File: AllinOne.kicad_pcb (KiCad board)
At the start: 2 copper layers, 24 parts, among them SW0 SW_Push, SW1 SW_Push, SW2 SW_Push, SW3 SW_Push, U1 ATmega32U4-A, Y1 16MHz

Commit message: Started organizing switches
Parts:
- removed D2, D3, D4: SOD-123, Diode_SMD:D_SOD-123
- added D10: SOD-123, Diode_SMD:D_SOD-123, F.Cu at (370.4, 227.7)
- added D100: SOD-123, Diode_SMD:D_SOD-123, F.Cu at (405.2, 227.7)
- added D101: SOD-123, Diode_SMD:D_SOD-123, F.Cu at (405.2, 231.0)
- added D102: SOD-123, Diode_SMD:D_SOD-123, F.Cu at (405.2, 234.4)
- added D103: SOD-123, Diode_SMD:D_SOD-123, F.Cu at (405.2, 237.7)
- added D104: SOD-123, Diode_SMD:D_SOD-123, F.Cu at (405.2, 241.1)
- added D105: SOD-123, Diode_SMD:D_SOD-123, F.Cu at (405.2, 244.4)
- added D106: SOD-123, Diode_SMD:D_SOD-123, F.Cu at (405.2, 247.8)
- added D107: SOD-123, Diode_SMD:D_SOD-123, F.Cu at (405.2, 251.1)
- added D108: SOD-123, Diode_SMD:D_SOD-123, F.Cu at (411.0, 207.6)
- added D109: SOD-123, Diode_SMD:D_SOD-123, F.Cu at (411.0, 210.9)
- added D11: SOD-123, Diode_SMD:D_SOD-123, F.Cu at (370.4, 231.0)
- added D110: SOD-123, Diode_SMD:D_SOD-123, F.Cu at (411.0, 214.3)
- added D111: SOD-123, Diode_SMD:D_SOD-123, F.Cu at (411.0, 217.6)
- added D112: SOD-123, Diode_SMD:D_SOD-123, F.Cu at (411.0, 221.0)
- added D113: SOD-123, Diode_SMD:D_SOD-123, F.Cu at (411.0, 224.3)
- added D114: SOD-123, Diode_SMD:D_SOD-123, F.Cu at (411.0, 227.7)
- added D115: SOD-123, Diode_SMD:D_SOD-123, F.Cu at (411.0, 231.0)
- added D116: SOD-123, Diode_SMD:D_SOD-123, F.Cu at (411.0, 234.4)
- added D119: SOD-123, Diode_SMD:D_SOD-123, F.Cu at (411.0, 237.7)
- added D12: SOD-123, Diode_SMD:D_SOD-123, F.Cu at (370.4, 234.4)
- added D121: SOD-123, Diode_SMD:D_SOD-123, F.Cu at (411.0, 241.1)
- added D122: SOD-123, Diode_SMD:D_SOD-123, F.Cu at (411.0, 244.4)
- added D123: SOD-123, Diode_SMD:D_SOD-123, F.Cu at (411.0, 247.8)
- added D124: SOD-123, Diode_SMD:D_SOD-123, F.Cu at (411.0, 251.1)
- added D125: SOD-123, Diode_SMD:D_SOD-123, F.Cu at (416.8, 207.6)
- added D126: SOD-123, Diode_SMD:D_SOD-123, F.Cu at (416.8, 210.9)
- added D127: SOD-123, Diode_SMD:D_SOD-123, F.Cu at (416.8, 214.3)
- added D13: SOD-123, Diode_SMD:D_SOD-123, F.Cu at (370.4, 237.7)
- added D131: SOD-123, Diode_SMD:D_SOD-123, F.Cu at (416.8, 217.6)
- added D135: SOD-123, Diode_SMD:D_SOD-123, F.Cu at (416.8, 221.0)
- added D136: SOD-123, Diode_SMD:D_SOD-123, F.Cu at (416.8, 224.3)
- added D137: SOD-123, Diode_SMD:D_SOD-123, F.Cu at (416.8, 227.7)
- added D138: SOD-123, Diode_SMD:D_SOD-123, F.Cu at (416.8, 231.0)
- added D139: SOD-123, Diode_SMD:D_SOD-123, F.Cu at (416.8, 234.4)
- added D14: SOD-123, Diode_SMD:D_SOD-123, F.Cu at (370.4, 241.1)
- added D140: SOD-123, Diode_SMD:D_SOD-123, F.Cu at (416.8, 237.7)
- added D141: SOD-123, Diode_SMD:D_SOD-123, F.Cu at (416.8, 241.1)
- added D142: SOD-123, Diode_SMD:D_SOD-123, F.Cu at (416.8, 244.4)
- added D143: SOD-123, Diode_SMD:D_SOD-123, F.Cu at (416.8, 247.8)
- added D144: SOD-123, Diode_SMD:D_SOD-123, F.Cu at (416.8, 251.1)
- added D15: SOD-123, Diode_SMD:D_SOD-123, F.Cu at (370.4, 244.4)
- added D16: SOD-123, Diode_SMD:D_SOD-123, F.Cu at (370.4, 247.8)
- added D17: SOD-123, Diode_SMD:D_SOD-123, F.Cu at (370.4, 251.1)
- added D18: SOD-123, Diode_SMD:D_SOD-123, F.Cu at (376.2, 207.6)
- added D19: SOD-123, Diode_SMD:D_SOD-123, F.Cu at (376.2, 210.9)
- added D20: SOD-123, Diode_SMD:D_SOD-123, F.Cu at (376.2, 214.3)
- added D23: SOD-123, Diode_SMD:D_SOD-123, F.Cu at (376.2, 217.6)
- added D24: SOD-123, Diode_SMD:D_SOD-123, F.Cu at (376.2, 221.0)
- added D25: SOD-123, Diode_SMD:D_SOD-123, F.Cu at (376.2, 224.3)
- added D26: SOD-123, Diode_SMD:D_SOD-123, F.Cu at (376.2, 227.7)
- added D27: SOD-123, Diode_SMD:D_SOD-123, F.Cu at (376.2, 231.0)
- added D28: SOD-123, Diode_SMD:D_SOD-123, F.Cu at (376.2, 234.4)
- added D29: SOD-123, Diode_SMD:D_SOD-123, F.Cu at (376.2, 237.7)
- added D30: SOD-123, Diode_SMD:D_SOD-123, F.Cu at (376.2, 241.1)
- added D31: SOD-123, Diode_SMD:D_SOD-123, F.Cu at (376.2, 244.4)
- added D32: SOD-123, Diode_SMD:D_SOD-123, F.Cu at (376.2, 247.8)
- added D33: SOD-123, Diode_SMD:D_SOD-123, F.Cu at (376.2, 251.1)
- added D34: SOD-123, Diode_SMD:D_SOD-123, F.Cu at (382.0, 207.6)
- added D35: SOD-123, Diode_SMD:D_SOD-123, F.Cu at (382.0, 210.9)
- added D36: SOD-123, Diode_SMD:D_SOD-123, F.Cu at (382.0, 214.3)
- added D37: SOD-123, Diode_SMD:D_SOD-123, F.Cu at (382.0, 217.6)
- added D38: SOD-123, Diode_SMD:D_SOD-123, F.Cu at (382.0, 221.0)
- added D39: SOD-123, Diode_SMD:D_SOD-123, F.Cu at (382.0, 224.3)
- added D40: SOD-123, Diode_SMD:D_SOD-123, F.Cu at (382.0, 227.7)
- added D41: SOD-123, Diode_SMD:D_SOD-123, F.Cu at (382.0, 231.0)
- added D42: SOD-123, Diode_SMD:D_SOD-123, F.Cu at (382.0, 234.4)
- added D43: SOD-123, Diode_SMD:D_SOD-123, F.Cu at (382.0, 237.7)
- added D44: SOD-123, Diode_SMD:D_SOD-123, F.Cu at (382.0, 241.1)
- added D45: SOD-123, Diode_SMD:D_SOD-123, F.Cu at (382.0, 244.4)
- added D46: SOD-123, Diode_SMD:D_SOD-123, F.Cu at (382.0, 247.8)
- added D47: SOD-123, Diode_SMD:D_SOD-123, F.Cu at (382.0, 251.1)
- added D48: SOD-123, Diode_SMD:D_SOD-123, F.Cu at (387.8, 207.6)
- added D49: SOD-123, Diode_SMD:D_SOD-123, F.Cu at (387.8, 210.9)
- added D5: SOD-123, Diode_SMD:D_SOD-123, F.Cu at (370.4, 210.9)
- added D50: SOD-123, Diode_SMD:D_SOD-123, F.Cu at (387.8, 214.3)
- added D51: SOD-123, Diode_SMD:D_SOD-123, F.Cu at (387.8, 217.6)
- added D52: SOD-123, Diode_SMD:D_SOD-123, F.Cu at (387.8, 221.0)
- added D53: SOD-123, Diode_SMD:D_SOD-123, F.Cu at (387.8, 224.3)
- added D54: SOD-123, Diode_SMD:D_SOD-123, F.Cu at (387.8, 227.7)
- added D55: SOD-123, Diode_SMD:D_SOD-123, F.Cu at (387.8, 231.0)
- added D56: SOD-123, Diode_SMD:D_SOD-123, F.Cu at (387.8, 234.4)
- added D57: SOD-123, Diode_SMD:D_SOD-123, F.Cu at (387.8, 237.7)
- added D58: SOD-123, Diode_SMD:D_SOD-123, F.Cu at (387.8, 241.1)
- added D6: SOD-123, Diode_SMD:D_SOD-123, F.Cu at (370.4, 214.3)
- added D60: SOD-123, Diode_SMD:D_SOD-123, F.Cu at (387.8, 244.4)
- added D61: SOD-123, Diode_SMD:D_SOD-123, F.Cu at (387.8, 247.8)
- added D62: SOD-123, Diode_SMD:D_SOD-123, F.Cu at (387.8, 251.1)
- added D63: SOD-123, Diode_SMD:D_SOD-123, F.Cu at (393.6, 207.6)
- added D64: SOD-123, Diode_SMD:D_SOD-123, F.Cu at (393.6, 210.9)
- added D65: SOD-123, Diode_SMD:D_SOD-123, F.Cu at (393.6, 214.3)
- added D66: SOD-123, Diode_SMD:D_SOD-123, F.Cu at (393.6, 217.6)
- added D67: SOD-123, Diode_SMD:D_SOD-123, F.Cu at (393.6, 221.0)
- added D68: SOD-123, Diode_SMD:D_SOD-123, F.Cu at (393.6, 224.3)
- added D69: SOD-123, Diode_SMD:D_SOD-123, F.Cu at (393.6, 227.7)
- added D7: SOD-123, Diode_SMD:D_SOD-123, F.Cu at (370.4, 217.6)
- added D70: SOD-123, Diode_SMD:D_SOD-123, F.Cu at (393.6, 231.0)
- added D71: SOD-123, Diode_SMD:D_SOD-123, F.Cu at (393.6, 234.4)
- added D72: SOD-123, Diode_SMD:D_SOD-123, F.Cu at (393.6, 237.7)
- added D73: SOD-123, Diode_SMD:D_SOD-123, F.Cu at (393.6, 241.1)
- added D74: SOD-123, Diode_SMD:D_SOD-123, F.Cu at (393.6, 244.4)
- added D75: SOD-123, Diode_SMD:D_SOD-123, F.Cu at (393.6, 247.8)
- added D76: SOD-123, Diode_SMD:D_SOD-123, F.Cu at (393.6, 251.1)
- added D77: SOD-123, Diode_SMD:D_SOD-123, F.Cu at (399.4, 207.6)
- added D79: SOD-123, Diode_SMD:D_SOD-123, F.Cu at (399.4, 210.9)
- added D8: SOD-123, Diode_SMD:D_SOD-123, F.Cu at (370.4, 221.0)
- added D80: SOD-123, Diode_SMD:D_SOD-123, F.Cu at (399.4, 214.3)
- added D81: SOD-123, Diode_SMD:D_SOD-123, F.Cu at (399.4, 217.6)
- added D82: SOD-123, Diode_SMD:D_SOD-123, F.Cu at (399.4, 221.0)
- added D83: SOD-123, Diode_SMD:D_SOD-123, F.Cu at (399.4, 224.3)
- added D84: SOD-123, Diode_SMD:D_SOD-123, F.Cu at (399.4, 227.7)
- added D85: SOD-123, Diode_SMD:D_SOD-123, F.Cu at (399.4, 231.0)
- added D86: SOD-123, Diode_SMD:D_SOD-123, F.Cu at (399.4, 234.4)
- added D87: SOD-123, Diode_SMD:D_SOD-123, F.Cu at (399.4, 237.7)
- added D88: SOD-123, Diode_SMD:D_SOD-123, F.Cu at (399.4, 241.1)
- added D89: SOD-123, Diode_SMD:D_SOD-123, F.Cu at (399.4, 244.4)
- added D9: SOD-123, Diode_SMD:D_SOD-123, F.Cu at (370.4, 224.3)
- added D90: SOD-123, Diode_SMD:D_SOD-123, F.Cu at (399.4, 247.8)
- added D91: SOD-123, Diode_SMD:D_SOD-123, F.Cu at (399.4, 251.1)
- added D92: SOD-123, Diode_SMD:D_SOD-123, F.Cu at (405.2, 207.6)
- added D93: SOD-123, Diode_SMD:D_SOD-123, F.Cu at (405.2, 210.9)
- added D94: SOD-123, Diode_SMD:D_SOD-123, F.Cu at (405.2, 214.3)
- added D95: SOD-123, Diode_SMD:D_SOD-123, F.Cu at (405.2, 217.6)
- added D96: SOD-123, Diode_SMD:D_SOD-123, F.Cu at (405.2, 221.0)
- added D97: SOD-123, Diode_SMD:D_SOD-123, F.Cu at (405.2, 224.3)
- added SW10: SW_Push, Button_Switch_Keyboard:SW_Cherry_MX_1.00u_PCB, F.Cu at (226.1, 87.2)
- added SW100: SW_Push, Button_Switch_Keyboard:SW_Cherry_MX_1.00u_PCB, F.Cu at (319.5, 168.6)
- added SW101: SW_Push, Button_Switch_Keyboard:SW_Cherry_MX_1.00u_PCB, F.Cu at (319.5, 188.8)
- added SW102: SW_Push, Button_Switch_Keyboard:SW_Cherry_MX_1.00u_PCB, F.Cu at (319.5, 209.0)
- added SW103: SW_Push, Button_Switch_Keyboard:SW_Cherry_MX_1.00u_PCB, F.Cu at (319.5, 229.2)
- added SW104: SW_Push, Button_Switch_Keyboard:SW_Cherry_MX_1.00u_PCB, F.Cu at (319.5, 249.4)
- added SW105: SW_Push, Button_Switch_Keyboard:SW_Cherry_MX_1.00u_PCB, F.Cu at (319.5, 269.6)
- added SW106: SW_Push, Button_Switch_Keyboard:SW_Cherry_MX_1.00u_PCB, F.Cu at (319.5, 289.8)
- added SW107: SW_Push, Button_Switch_Keyboard:SW_Cherry_MX_1.00u_PCB, F.Cu at (319.5, 310.0)
- added SW108: SW_Push, Button_Switch_Keyboard:SW_Cherry_MX_1.00u_PCB, F.Cu at (319.5, 330.2)
- added SW109: SW_Push, Button_Switch_Keyboard:SW_Cherry_MX_1.00u_PCB, F.Cu at (319.5, 350.4)
- added SW11: SW_Push, Button_Switch_Keyboard:SW_Cherry_MX_1.00u_PCB, F.Cu at (245.1, 87.2)
- added SW110: SW_Push, Button_Switch_Keyboard:SW_Cherry_MX_1.00u_PCB, F.Cu at (319.5, 370.6)
- added SW111: SW_Push, Button_Switch_Keyboard:SW_Cherry_MX_1.00u_PCB, F.Cu at (319.5, 390.8)
- added SW114: SW_Push, Button_Switch_Keyboard:SW_Cherry_MX_1.00u_PCB, F.Cu at (339.5, 144.4)
- added SW116: SW_Push, Button_Switch_Keyboard:SW_Cherry_MX_1.00u_PCB, F.Cu at (339.7, 168.6)
- added SW117: SW_Push, Button_Switch_Keyboard:SW_Cherry_MX_1.00u_PCB, F.Cu at (339.7, 188.8)
- added SW118: SW_Push, Button_Switch_Keyboard:SW_Cherry_MX_1.00u_PCB, F.Cu at (339.7, 209.0)
- added SW119: SW_Push, Button_Switch_Keyboard:SW_Cherry_MX_1.00u_PCB, F.Cu at (339.7, 229.2)
- added SW12: SW_Push, Button_Switch_Keyboard:SW_Cherry_MX_1.00u_PCB, F.Cu at (264.2, 87.2)
- added SW120: SW_Push, Button_Switch_Keyboard:SW_Cherry_MX_1.00u_PCB, F.Cu at (339.7, 249.4)
- added SW121: SW_Push, Button_Switch_Keyboard:SW_Cherry_MX_1.00u_PCB, F.Cu at (339.7, 269.6)
- added SW122: SW_Push, Button_Switch_Keyboard:SW_Cherry_MX_1.00u_PCB, F.Cu at (339.7, 289.8)
- added SW126: SW_Push, Button_Switch_Keyboard:SW_Cherry_MX_6.25u_PCB, F.Cu at (228.1, 411.0)
- added SW13: SW_Push, Button_Switch_Keyboard:SW_Cherry_MX_1.00u_PCB, F.Cu at (283.2, 87.2)
- added SW130: SW_Push, Button_Switch_Keyboard:SW_Cherry_MX_1.00u_PCB, F.Cu at (339.7, 310.0)
- added SW131: SW_Push, Button_Switch_Keyboard:SW_Cherry_MX_1.00u_PCB, F.Cu at (339.7, 330.2)
- added SW132: SW_Push, Button_Switch_Keyboard:SW_Cherry_MX_1.00u_PCB, F.Cu at (339.7, 350.4)
- added SW133: SW_Push, Button_Switch_Keyboard:SW_Cherry_MX_1.00u_PCB, F.Cu at (339.7, 370.6)
- added SW134: SW_Push, Button_Switch_Keyboard:SW_Cherry_MX_1.00u_PCB, F.Cu at (339.7, 390.8)
- added SW135: SW_Push, Button_Switch_Keyboard:SW_Cherry_MX_1.00u_PCB, F.Cu at (358.5, 144.4)
- added SW136: SW_Push, Button_Switch_Keyboard:SW_Cherry_MX_1.00u_PCB, F.Cu at (359.9, 168.6)
- added SW137: SW_Push, Button_Switch_Keyboard:SW_Cherry_MX_1.00u_PCB, F.Cu at (359.9, 188.8)
- added SW138: SW_Push, Button_Switch_Keyboard:SW_Cherry_MX_1.00u_PCB, F.Cu at (359.9, 209.0)
- added SW139: SW_Push, Button_Switch_Keyboard:SW_Cherry_MX_1.00u_PCB, F.Cu at (359.9, 229.2)
- added SW14: SW_Push, Button_Switch_Keyboard:SW_Cherry_MX_1.00u_PCB, F.Cu at (302.3, 87.2)
- added SW15: SW_Push, Button_Switch_Keyboard:SW_Cherry_MX_1.00u_PCB, F.Cu at (321.3, 87.2)
- added SW16: SW_Push, Button_Switch_Keyboard:SW_Cherry_MX_2.00u_PCB, F.Cu at (389.7, 148.4)
- added SW18: SW_Push, Button_Switch_Keyboard:SW_Cherry_MX_1.00u_PCB, F.Cu at (378.5, 87.2)
- added SW19: SW_Push, Button_Switch_Keyboard:SW_Cherry_MX_1.00u_PCB, F.Cu at (397.5, 87.2)
- added SW20: SW_Push, Button_Switch_Keyboard:SW_Cherry_MX_1.00u_PCB, F.Cu at (35.6, 106.3)
- added SW21: SW_Push, Button_Switch_Keyboard:SW_Cherry_MX_1.00u_PCB, F.Cu at (54.6, 106.3)
- added SW22: SW_Push, Button_Switch_Keyboard:SW_Cherry_MX_1.00u_PCB, F.Cu at (73.7, 106.3)
- added SW23: SW_Push, Button_Switch_Keyboard:SW_Cherry_MX_1.00u_PCB, F.Cu at (92.7, 106.3)
- added SW24: SW_Push, Button_Switch_Keyboard:SW_Cherry_MX_1.00u_PCB, F.Cu at (111.8, 106.3)
- added SW25: SW_Push, Button_Switch_Keyboard:SW_Cherry_MX_1.00u_PCB, F.Cu at (130.8, 106.3)
- added SW26: SW_Push, Button_Switch_Keyboard:SW_Cherry_MX_1.00u_PCB, F.Cu at (149.9, 106.3)
- added SW27: SW_Push, Button_Switch_Keyboard:SW_Cherry_MX_1.00u_PCB, F.Cu at (168.9, 106.3)
- added SW28: SW_Push, Button_Switch_Keyboard:SW_Cherry_MX_1.00u_PCB, F.Cu at (218.5, 148.4)
- added SW29: SW_Push, Button_Switch_Keyboard:SW_Cherry_MX_1.00u_PCB, F.Cu at (218.5, 168.6)
- added SW30: SW_Push, Button_Switch_Keyboard:SW_Cherry_MX_1.00u_PCB, F.Cu at (218.5, 188.8)
- added SW31: SW_Push, Button_Switch_Keyboard:SW_Cherry_MX_1.00u_PCB, F.Cu at (218.5, 209.0)
- added SW32: SW_Push, Button_Switch_Keyboard:SW_Cherry_MX_1.00u_PCB, F.Cu at (218.5, 229.2)
- added SW33: SW_Push, Button_Switch_Keyboard:SW_Cherry_MX_1.00u_PCB, F.Cu at (218.5, 249.4)
- added SW34: SW_Push, Button_Switch_Keyboard:SW_Cherry_MX_1.00u_PCB, F.Cu at (218.5, 269.6)
- added SW35: SW_Push, Button_Switch_Keyboard:SW_Cherry_MX_1.00u_PCB, F.Cu at (218.5, 289.8)
- added SW36: SW_Push, Button_Switch_Keyboard:SW_Cherry_MX_1.00u_PCB, F.Cu at (218.5, 310.0)
- added SW37: SW_Push, Button_Switch_Keyboard:SW_Cherry_MX_1.00u_PCB, F.Cu at (218.5, 330.2)
- added SW38: SW_Push, Button_Switch_Keyboard:SW_Cherry_MX_1.00u_PCB, F.Cu at (218.5, 350.4)
- added SW39: SW_Push, Button_Switch_Keyboard:SW_Cherry_MX_1.00u_PCB, F.Cu at (218.5, 370.6)
- added SW4: SW_Push, Button_Switch_Keyboard:SW_Cherry_MX_1.00u_PCB, F.Cu at (111.8, 87.2)
- added SW40: SW_Push, Button_Switch_Keyboard:SW_Cherry_MX_1.00u_PCB, F.Cu at (218.5, 390.8)
- added SW41: SW_Push, Button_Switch_Keyboard:SW_Cherry_MX_1.00u_PCB, F.Cu at (238.7, 148.4)
- added SW42: SW_Push, Button_Switch_Keyboard:SW_Cherry_MX_1.00u_PCB, F.Cu at (238.7, 168.6)
- added SW43: SW_Push, Button_Switch_Keyboard:SW_Cherry_MX_1.00u_PCB, F.Cu at (238.7, 188.8)
- added SW44: SW_Push, Button_Switch_Keyboard:SW_Cherry_MX_1.00u_PCB, F.Cu at (238.7, 209.0)
- added SW45: SW_Push, Button_Switch_Keyboard:SW_Cherry_MX_1.00u_PCB, F.Cu at (238.7, 229.2)
- added SW46: SW_Push, Button_Switch_Keyboard:SW_Cherry_MX_1.00u_PCB, F.Cu at (238.7, 249.4)
- added SW47: SW_Push, Button_Switch_Keyboard:SW_Cherry_MX_1.00u_PCB, F.Cu at (238.7, 269.6)
- added SW48: SW_Push, Button_Switch_Keyboard:SW_Cherry_MX_1.00u_PCB, F.Cu at (238.7, 289.8)
- added SW49: SW_Push, Button_Switch_Keyboard:SW_Cherry_MX_1.00u_PCB, F.Cu at (238.7, 310.0)
- added SW5: SW_Push, Button_Switch_Keyboard:SW_Cherry_MX_1.00u_PCB, F.Cu at (130.8, 87.2)
- added SW50: SW_Push, Button_Switch_Keyboard:SW_Cherry_MX_1.00u_PCB, F.Cu at (238.7, 330.2)
- added SW51: SW_Push, Button_Switch_Keyboard:SW_Cherry_MX_1.00u_PCB, F.Cu at (238.7, 350.4)
- added SW52: SW_Push, Button_Switch_Keyboard:SW_Cherry_MX_1.00u_PCB, F.Cu at (238.7, 370.6)
- added SW53: SW_Push, Button_Switch_Keyboard:SW_Cherry_MX_2.00u_PCB, F.Cu at (389.7, 169.3)
- added SW55: SW_Push, Button_Switch_Keyboard:SW_Cherry_MX_1.00u_PCB, F.Cu at (238.7, 390.8)
- added SW56: SW_Push, Button_Switch_Keyboard:SW_Cherry_MX_1.00u_PCB, F.Cu at (258.9, 148.4)
- added SW57: SW_Push, Button_Switch_Keyboard:SW_Cherry_MX_1.00u_PCB, F.Cu at (258.9, 168.6)
- added SW58: SW_Push, Button_Switch_Keyboard:SW_Cherry_MX_1.00u_PCB, F.Cu at (258.9, 188.8)
- added SW59: SW_Push, Button_Switch_Keyboard:SW_Cherry_MX_1.00u_PCB, F.Cu at (258.9, 209.0)
- added SW6: SW_Push, Button_Switch_Keyboard:SW_Cherry_MX_1.00u_PCB, F.Cu at (149.9, 87.2)
- added SW60: SW_Push, Button_Switch_Keyboard:SW_Cherry_MX_1.00u_PCB, F.Cu at (258.9, 229.2)
- added SW61: SW_Push, Button_Switch_Keyboard:SW_Cherry_MX_1.00u_PCB, F.Cu at (258.9, 249.4)
- added SW62: SW_Push, Button_Switch_Keyboard:SW_Cherry_MX_1.00u_PCB, F.Cu at (258.9, 269.6)
- added SW63: SW_Push, Button_Switch_Keyboard:SW_Cherry_MX_1.00u_PCB, F.Cu at (258.9, 289.8)
- added SW64: SW_Push, Button_Switch_Keyboard:SW_Cherry_MX_1.00u_PCB, F.Cu at (258.9, 310.0)
- added SW65: SW_Push, Button_Switch_Keyboard:SW_Cherry_MX_1.00u_PCB, F.Cu at (258.9, 330.2)
- added SW66: SW_Push, Button_Switch_Keyboard:SW_Cherry_MX_1.00u_PCB, F.Cu at (258.9, 350.4)
- added SW67: SW_Push, Button_Switch_Keyboard:SW_Cherry_MX_1.00u_PCB, F.Cu at (258.9, 370.6)
- added SW68: SW_Push, Button_Switch_Keyboard:SW_Cherry_MX_1.00u_PCB, F.Cu at (258.9, 390.8)
- added SW69: SW_Push, Button_Switch_Keyboard:SW_Cherry_MX_1.00u_PCB, F.Cu at (279.1, 148.4)
- added SW7: SW_Push, Button_Switch_Keyboard:SW_Cherry_MX_1.00u_PCB, F.Cu at (168.9, 87.2)
- added SW70: SW_Push, Button_Switch_Keyboard:SW_Cherry_MX_1.00u_PCB, F.Cu at (279.1, 168.6)
- added SW71: SW_Push, Button_Switch_Keyboard:SW_Cherry_MX_1.00u_PCB, F.Cu at (279.1, 188.8)
- added SW72: SW_Push, Button_Switch_Keyboard:SW_Cherry_MX_1.00u_PCB, F.Cu at (279.1, 209.0)
- added SW74: SW_Push, Button_Switch_Keyboard:SW_Cherry_MX_2.00u_PCB, F.Cu at (389.7, 190.1)
- added SW75: SW_Push, Button_Switch_Keyboard:SW_Cherry_MX_1.00u_PCB, F.Cu at (279.1, 229.2)
- added SW76: SW_Push, Button_Switch_Keyboard:SW_Cherry_MX_1.00u_PCB, F.Cu at (279.1, 249.4)
- added SW77: SW_Push, Button_Switch_Keyboard:SW_Cherry_MX_1.00u_PCB, F.Cu at (279.1, 269.6)
- added SW78: SW_Push, Button_Switch_Keyboard:SW_Cherry_MX_1.00u_PCB, F.Cu at (279.1, 289.8)
- added SW79: SW_Push, Button_Switch_Keyboard:SW_Cherry_MX_1.00u_PCB, F.Cu at (279.1, 310.0)
- added SW8: SW_Push, Button_Switch_Keyboard:SW_Cherry_MX_1.00u_PCB, F.Cu at (188.0, 87.2)
- added SW80: SW_Push, Button_Switch_Keyboard:SW_Cherry_MX_1.00u_PCB, F.Cu at (279.1, 330.2)
- added SW81: SW_Push, Button_Switch_Keyboard:SW_Cherry_MX_1.00u_PCB, F.Cu at (279.1, 350.4)
- added SW82: SW_Push, Button_Switch_Keyboard:SW_Cherry_MX_1.00u_PCB, F.Cu at (279.1, 370.6)
- added SW83: SW_Push, Button_Switch_Keyboard:SW_Cherry_MX_1.00u_PCB, F.Cu at (279.1, 390.8)
- added SW84: SW_Push, Button_Switch_Keyboard:SW_Cherry_MX_1.00u_PCB, F.Cu at (299.3, 148.4)
- added SW85: SW_Push, Button_Switch_Keyboard:SW_Cherry_MX_1.00u_PCB, F.Cu at (299.3, 168.6)
- added SW86: SW_Push, Button_Switch_Keyboard:SW_Cherry_MX_1.00u_PCB, F.Cu at (299.3, 188.8)
- added SW87: SW_Push, Button_Switch_Keyboard:SW_Cherry_MX_1.00u_PCB, F.Cu at (299.3, 209.0)
- added SW88: SW_Push, Button_Switch_Keyboard:SW_Cherry_MX_1.00u_PCB, F.Cu at (299.3, 229.2)
- added SW89: SW_Push, Button_Switch_Keyboard:SW_Cherry_MX_1.00u_PCB, F.Cu at (299.3, 249.4)
- added SW9: SW_Push, Button_Switch_Keyboard:SW_Cherry_MX_1.00u_PCB, F.Cu at (207.0, 87.2)
- added SW90: SW_Push, Button_Switch_Keyboard:SW_Cherry_MX_1.00u_PCB, F.Cu at (299.3, 269.6)
- added SW91: SW_Push, Button_Switch_Keyboard:SW_Cherry_MX_1.00u_PCB, F.Cu at (299.3, 289.8)
- added SW92: SW_Push, Button_Switch_Keyboard:SW_Cherry_MX_1.00u_PCB, F.Cu at (299.3, 310.0)
- added SW95: SW_Push, Button_Switch_Keyboard:SW_Cherry_MX_1.00u_PCB, F.Cu at (299.3, 330.2)
- added SW96: SW_Push, Button_Switch_Keyboard:SW_Cherry_MX_1.00u_PCB, F.Cu at (299.3, 350.4)
- added SW97: SW_Push, Button_Switch_Keyboard:SW_Cherry_MX_1.00u_PCB, F.Cu at (299.3, 370.6)
- added SW98: SW_Push, Button_Switch_Keyboard:SW_Cherry_MX_1.00u_PCB, F.Cu at (299.3, 390.8)
- added SW99: SW_Push, Button_Switch_Keyboard:SW_Cherry_MX_1.00u_PCB, F.Cu at (319.5, 148.4)
- D1: moved to F.Cu
- moved D1 301.7 mm to (370.4, 207.6), turned to 0 degrees
- moved SW0 93.3 mm to (35.6, 87.2)
- moved SW1 93.3 mm to (54.6, 87.2)
- moved SW2 51.2 mm to (73.7, 87.2)
- moved SW3 51.2 mm to (92.7, 87.2)
- moved C2 36.6 mm to (46.0, 59.7)
- moved C1 36.6 mm to (29.5, 50.3)
- moved C3 36.6 mm to (50.3, 46.0)
- moved C4 36.6 mm to (31.8, 42.4)
- moved C6 36.6 mm to (45.2, 38.4)
- moved F1 36.6 mm to (18.8, 45.2)
- moved R1 36.6 mm to (50.8, 56.6)
- moved R3 36.6 mm to (23.4, 35.3)
- moved R4 36.6 mm to (28.2, 42.4)
- moved USB1 36.6 mm to (25.4, 23.1)
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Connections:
- D1 pad 1: ROW_0 -> ROW_6
- SW0 pad 1: Net-(D1-A) -> Net-(D5-A)
- SW1 pad 2: COL_1 -> COL_0
- SW2 pad 2: COL_0 -> COL_1

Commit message: Finished switch lineup
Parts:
- SW111: footprint Button_Switch_Keyboard:SW_Cherry_MX_1.00u_PCB -> Button_Switch_Keyboard:SW_Cherry_MX_2.00u_PCB
- moved D1 347.5 mm to (42.5, 92.6)
- moved SW40 322.4 mm to (35.6, 125.3)
- moved SW39 319.2 mm to (397.5, 106.3)
- moved SW120 307.9 mm to (35.6, 201.5)
- moved SW80 295.2 mm to (35.6, 163.4)
- moved SW83 294.0 mm to (92.7, 163.4)
- moved SW121 293.1 mm to (54.6, 201.5)
- moved SW81 292.2 mm to (54.6, 163.4)
- moved SW38 291.8 mm to (378.5, 106.3)
- moved SW82 291.8 mm to (73.7, 163.4)
- moved SW100 284.3 mm to (35.6, 182.5)
- moved SW122 280.3 mm to (73.7, 201.5)
- moved SW55 278.0 mm to (321.3, 125.3)
- moved D10 267.6 mm to (178.8, 40.9)
- moved D100 267.6 mm to (213.6, 40.9)
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
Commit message: Started diode placement
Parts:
- moved D1 268.0 mm to (304.5, 149.1)
- moved D5 153.9 mm to (41.4, 93.5), turned to 90 degrees
- moved D6 135.5 mm to (60.5, 93.5), turned to 90 degrees
- moved D7 117.4 mm to (79.5, 93.5), turned to 90 degrees
- moved D8 99.8 mm to (98.5, 93.5), turned to 90 degrees
- moved D17 95.7 mm to (270.0, 93.5), turned to 90 degrees
- moved D9 83.0 mm to (117.6, 93.5), turned to 90 degrees
- moved D16 79.1 mm to (251.0, 93.5), turned to 90 degrees
- moved D10 67.4 mm to (136.7, 93.5), turned to 90 degrees
- moved D15 64.1 mm to (231.9, 93.5), turned to 90 degrees
- moved D11 54.4 mm to (155.7, 93.5), turned to 90 degrees
- moved D14 51.9 mm to (212.9, 93.5), turned to 90 degrees
- moved D12 46.1 mm to (174.8, 93.5), turned to 90 degrees
- moved D125 45.5 mm to (179.7, 19.9), turned to 90 degrees
- moved D13 45.1 mm to (193.8, 93.5), turned to 90 degrees
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
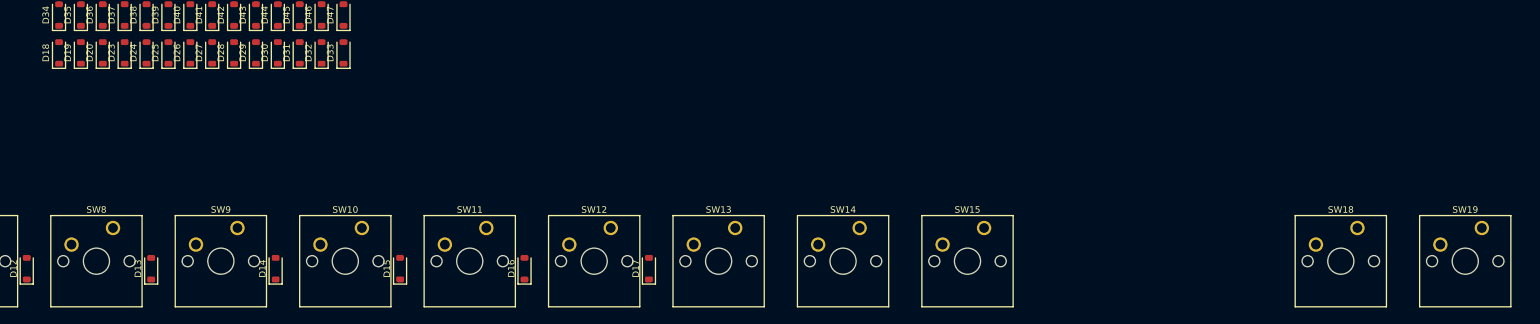
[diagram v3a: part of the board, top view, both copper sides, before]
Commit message: Finished one row of diodes
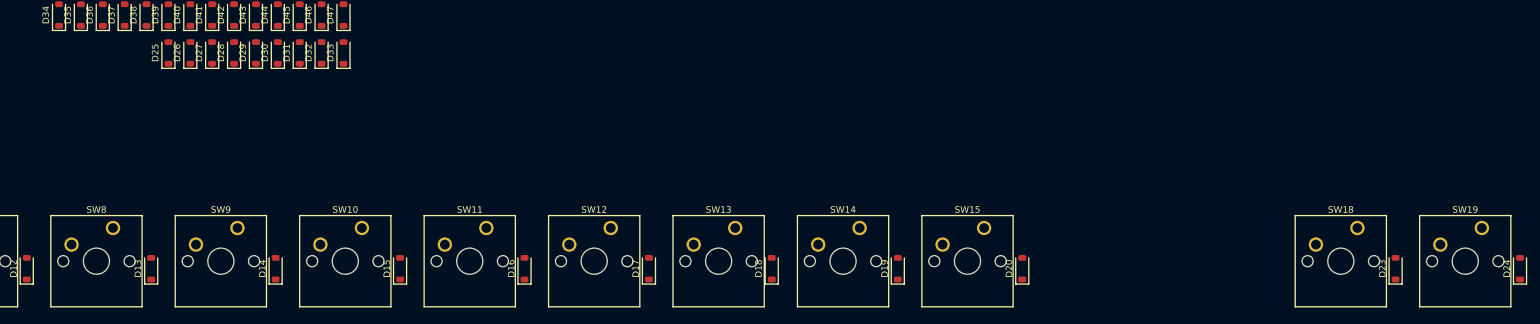
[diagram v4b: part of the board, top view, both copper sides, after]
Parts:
- moved D24 212.8 mm to (403.4, 93.5)
- moved D23 197.3 mm to (384.3, 93.5)
- moved D20 144.6 mm to (327.2, 93.5)
- moved D19 129.3 mm to (308.1, 93.5)
- moved D18 114.0 mm to (288.8, 93.5)
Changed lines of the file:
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@@
   )
   (footprint "Diode_SMD:D_SOD-123" (layer "F.Cu")
-    (at 183.042 60.445 90)
+    (at 308.102 93.472 90)
     (descr "SOD-123")
     (tags "SOD-123")
@@
   )
   (footprint "Diode_SMD:D_SOD-123" (layer "F.Cu")
-    (at 179.692 60.445 90)
+    (at 288.798 93.472 90)
     (descr "SOD-123")
     (tags "SOD-123")
@@
   )
   (footprint "Diode_SMD:D_SOD-123" (layer "F.Cu")
-    (at 189.742 60.445 90)
+    (at 384.302 93.472 90)
     (descr "SOD-123")
     (tags "SOD-123")
@@
   )
   (footprint "Diode_SMD:D_SOD-123" (layer "F.Cu")
-    (at 193.092 60.445 90)
+    (at 403.352 93.472 90)
     (descr "SOD-123")
     (tags "SOD-123")
@@
   )
   (footprint "Diode_SMD:D_SOD-123" (layer "F.Cu")
-    (at 186.392 60.445 90)
+    (at 327.152 93.472 90)
     (descr "SOD-123")
     (tags "SOD-123")

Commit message: Halfway done with diodes
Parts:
- moved C1 312.0 mm to (340.3, 77.3)
- moved C2 312.0 mm to (356.8, 86.7)
- moved C3 312.0 mm to (361.1, 73.0)
- moved C4 312.0 mm to (342.6, 69.5)
- moved C6 312.0 mm to (356.0, 65.4)
- moved F1 312.0 mm to (329.6, 72.3)
- moved R1 312.0 mm to (361.6, 83.7)
- moved R2 312.0 mm to (337.5, 62.4)
- moved R3 312.0 mm to (334.2, 62.4)
- moved R4 312.0 mm to (339.0, 69.5)
- moved SW_R1 312.0 mm to (339.2, 88.3)
- moved USB1 312.0 mm to (336.2, 50.2)
- moved Y1 312.0 mm to (351.7, 65.4)
- moved C5 312.0 mm to (347.4, 87.0)
- moved C7 312.0 mm to (347.4, 65.4)
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
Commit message: Finished now just wire
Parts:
- moved D104 198.6 mm to (403.4, 169.7)
- moved D105 194.3 mm to (41.4, 188.7)
- moved D103 184.3 mm to (384.3, 169.7)
- moved D124 180.2 mm to (403.4, 188.7)
- moved D106 179.5 mm to (60.5, 188.7)
- moved D144 174.0 mm to (403.4, 207.8)
- moved D102 170.4 mm to (365.3, 169.7)
- moved D123 165.3 mm to (384.3, 188.7)
- moved D107 164.8 mm to (79.5, 188.7)
- moved D143 158.6 mm to (384.3, 207.8)
- moved D101 156.8 mm to (346.2, 169.7)
- moved D122 150.7 mm to (365.3, 188.7)
- moved D125 150.6 mm to (41.4, 207.8)
- moved D142 143.3 mm to (365.3, 207.8)
- moved D121 136.2 mm to (346.2, 188.7)
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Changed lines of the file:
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@@
   )
   (footprint "Diode_SMD:D_SOD-123" (layer "F.Cu")
-    (at 208.74 245.031 90)
+    (at 212.852 188.722 90)
     (descr "SOD-123")
     (tags "SOD-123")
@@
   )
   (footprint "Diode_SMD:D_SOD-123" (layer "F.Cu")
-    (at 215.44 245.031 90)
+    (at 262.001 188.722 90)
     (descr "SOD-123")
     (tags "SOD-123")
@@
   )
   (footprint "Diode_SMD:D_SOD-123" (layer "F.Cu")
-    (at 222.14 245.031 90)
+    (at 346.202 188.722 90)
     (descr "SOD-123")
     (tags "SOD-123")
@@
   )
   (footprint "Diode_SMD:D_SOD-123" (layer "F.Cu")
-    (at 225.49 245.031 90)
+    (at 365.252 188.722 90)
     (descr "SOD-123")
     (tags "SOD-123")
@@
   )
   (footprint "Diode_SMD:D_SOD-123" (layer "F.Cu")
-    (at 228.84 250.826 90)
+    (at 60.452 188.721 90)
     (descr "SOD-123")
     (tags "SOD-123")
@@
   )
   (footprint "Diode_SMD:D_SOD-123" (layer "F.Cu")
-    (at 232.19 245.031 90)
+    (at 403.352 188.722 90)
     (descr "SOD-123")
     (tags "SOD-123")
@@
   )
   (footprint "Diode_SMD:D_SOD-123" (layer "F.Cu")
-    (at 205.39 245.031 90)
+    (at 193.802 188.722 90)
     (descr "SOD-123")
     (tags "SOD-123")
@@
   )
   (footprint "Diode_SMD:D_SOD-123" (layer "F.Cu")
-    (at 212.09 250.826 90)
+    (at 346.202 169.671 90)
     (descr "SOD-123")
     (tags "SOD-123")
@@
   )
   (footprint "Diode_SMD:D_SOD-123" (layer "F.Cu")
-    (at 212.09 245.031 90)
+    (at 231.902 188.722 90)
     (descr "SOD-123")
     (tags "SOD-123")
@@
   )
   (footprint "Diode_SMD:D_SOD-123" (layer "F.Cu")
-    (at 202.04 245.031 90)
+    (at 174.752 188.722 90)
     (descr "SOD-123")
     (tags "SOD-123")
@@
   )
   (footprint "Diode_SMD:D_SOD-123" (layer "F.Cu")
-    (at 232.19 250.826 90)
+    (at 79.502 188.721 90)
     (descr "SOD-123")
     (tags "SOD-123")
@@
   )
   (footprint "Diode_SMD:D_SOD-123" (layer "F.Cu")
-    (at 208.74 239.236 90)
+    (at 270.002 207.772 90)
     (descr "SOD-123")
     (tags "SOD-123")
@@
   )
   (footprint "Diode_SMD:D_SOD-123" (layer "F.Cu")
-    (at 222.14 239.236 90)
+    (at 346.202 207.772 90)
     (descr "SOD-123")
     (tags "SOD-123")
@@
   )
   (footprint "Diode_SMD:D_SOD-123" (layer "F.Cu")
-    (at 188.64 239.236 90)
+    (at 41.402 207.772 90)
     (descr "SOD-123")
     (tags "SOD-123")
@@
   )
   (footprint "Diode_SMD:D_SOD-123" (layer "F.Cu")
-    (at 218.79 245.031 90)
+    (at 308.102 188.722 90)
     (descr "SOD-123")
     (tags "SOD-123")
@@
   )
   (footprint "Diode_SMD:D_SOD-123" (layer "F.Cu")
-    (at 228.84 239.236 90)
+    (at 384.302 207.772 90)
     (descr "SOD-123")
     (tags "SOD-123")
@@
   )
   (footprint "Diode_SMD:D_SOD-123" (layer "F.Cu")
-    (at 198.69 239.236 90)
+    (at 155.829 207.772 90)
     (descr "SOD-123")
     (tags "SOD-123")
@@
   )
   (footprint "Diode_SMD:D_SOD-123" (layer "F.Cu")
-    (at 215.44 239.236 90)
+    (at 308.102 207.772 90)
     (descr "SOD-123")
     (tags "SOD-123")
@@
   )
   (footprint "Diode_SMD:D_SOD-123" (layer "F.Cu")
-    (at 218.79 239.236 90)
+    (at 327.152 207.772 90)
     (descr "SOD-123")
     (tags "SOD-123")
@@
   )
   (footprint "Diode_SMD:D_SOD-123" (layer "F.Cu")
-    (at 195.34 245.031 90)
+    (at 136.652 188.722 90)
     (descr "SOD-123")
     (tags "SOD-123")
@@
   )
   (footprint "Diode_SMD:D_SOD-123" (layer "F.Cu")
-    (at 195.34 239.236 90)
+    (at 79.502 207.772 90)
     (descr "SOD-123")
     (tags "SOD-123")
@@
   )
   (footprint "Diode_SMD:D_SOD-123" (layer "F.Cu")
-    (at 222.14 250.826 90)
+    (at 403.352 169.671 90)
     (descr "SOD-123")
     (tags "SOD-123")
@@
   )
   (footprint "Diode_SMD:D_SOD-123" (layer "F.Cu")
-    (at 225.49 250.826 90)
+    (at 41.402 188.721 90)
     (descr "SOD-123")
     (tags "SOD-123")
@@
   )
   (footprint "Diode_SMD:D_SOD-123" (layer "F.Cu")
-    (at 205.39 239.236 90)
+    (at 250.952 207.772 90)
     (descr "SOD-123")
     (tags "SOD-123")
@@
   )
   (footprint "Diode_SMD:D_SOD-123" (layer "F.Cu")
-    (at 225.49 239.236 90)
+    (at 365.252 207.772 90)
     (descr "SOD-123")
     (tags "SOD-123")
@@
   )
   (footprint "Diode_SMD:D_SOD-123" (layer "F.Cu")
-    (at 198.69 245.031 90)
+    (at 155.702 188.722 90)
     (descr "SOD-123")
     (tags "SOD-123")
@@
   )
   (footprint "Diode_SMD:D_SOD-123" (layer "F.Cu")
-    (at 188.64 245.031 90)
+    (at 98.552 188.721 90)
     (descr "SOD-123")
     (tags "SOD-123")
@@
   )
   (footprint "Diode_SMD:D_SOD-123" (layer "F.Cu")
-    (at 218.79 250.826 90)
+    (at 384.302 169.671 90)
     (descr "SOD-123")
     (tags "SOD-123")
@@
   )
   (footprint "Diode_SMD:D_SOD-123" (layer "F.Cu")
-    (at 232.19 239.236 90)
+    (at 403.352 207.772 90)
     (descr "SOD-123")
     (tags "SOD-123")
@@
   )
   (footprint "Diode_SMD:D_SOD-123" (layer "F.Cu")
-    (at 191.99 245.031 90)
+    (at 117.602 188.721 90)
     (descr "SOD-123")
     (tags "SOD-123")
@@
   )
   (footprint "Diode_SMD:D_SOD-123" (layer "F.Cu")
-    (at 191.99 239.236 90)
+    (at 60.452 207.772 90)
     (descr "SOD-123")
     (tags "SOD-123")
@@
   )
   (footprint "Diode_SMD:D_SOD-123" (layer "F.Cu")
-    (at 215.44 250.826 90)
+    (at 365.252 169.671 90)
     (descr "SOD-123")
     (tags "SOD-123")
@@
   )
   (footprint "Diode_SMD:D_SOD-123" (layer "F.Cu")
-    (at 202.04 239.236 90)
+    (at 231.902 207.772 90)
     (descr "SOD-123")
     (tags "SOD-123")
@@
   )
   (footprint "Diode_SMD:D_SOD-123" (layer "F.Cu")
-    (at 212.09 239.236 90)
+    (at 289.052 207.772 90)
     (descr "SOD-123")
     (tags "SOD-123")
@@
   )
   (footprint "Diode_SMD:D_SOD-123" (layer "F.Cu")
-    (at 228.84 245.031 90)
+    (at 384.302 188.722 90)
     (descr "SOD-123")
     (tags "SOD-123")

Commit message: Started routing the rows and finished the columns
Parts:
- moved C3 6.22 mm to (362.2, 79.1)
- moved C4 6.22 mm to (343.7, 75.6)
- moved C5 6.22 mm to (348.5, 93.1)
- moved C7 6.22 mm to (348.5, 71.5)
- moved SW_R1 6.22 mm to (340.3, 94.4)
- moved USB1 6.22 mm to (337.3, 56.3)
- moved C1 6.22 mm to (341.4, 83.5)
- moved C6 6.22 mm to (357.1, 71.5)
- moved F1 6.22 mm to (330.7, 78.4)
- moved R4 6.22 mm to (340.1, 75.6)
- moved Y1 6.22 mm to (352.8, 71.5)
- moved U1 6.22 mm to (353.0, 84.0)
- moved R2 6.22 mm to (338.6, 68.5)
- moved R3 6.22 mm to (335.3, 68.5)
- moved C2 6.22 mm to (357.9, 92.9)
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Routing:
- net ROW_11: track 0.00 -> 371.5 mm
- net ROW_13: track 0.00 -> 369.7 mm
- net ROW_10: track 0.00 -> 365.6 mm, vias 0 -> 12
- net ROW_12: track 0.00 -> 365.1 mm, vias 0 -> 10
- net COL_9: track 0.00 -> 247.7 mm
- net COL_0: track 0.00 -> 247.7 mm
- net COL_7: track 0.00 -> 236.5 mm
- net COL_3: track 0.00 -> 228.6 mm
- net COL_1: track 0.00 -> 228.6 mm
- net COL_5: track 0.00 -> 228.6 mm
- net COL_8: track 0.00 -> 209.6 mm
- net COL_2: track 0.00 -> 209.6 mm
- net COL_4: track 0.00 -> 209.5 mm
- net COL_6: track 0.00 -> 179.3 mm
- net ROW_9: track 0.00 -> 88.0 mm
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
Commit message: almost done wiring all rows
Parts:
- moved C4 24.8 mm to (342.4, 50.8)
- moved R4 24.8 mm to (338.7, 50.8)
- moved C3 24.8 mm to (360.8, 54.3)
- moved C7 24.8 mm to (347.1, 46.7)
- moved USB1 24.8 mm to (335.9, 31.5)
- moved C1 24.8 mm to (340.0, 58.7)
- moved C6 24.8 mm to (355.8, 46.7)
- moved F1 24.8 mm to (329.3, 53.6)
- moved Y1 24.8 mm to (351.4, 46.7)
- moved C5 24.8 mm to (347.1, 68.3)
- moved R1 24.8 mm to (361.3, 65.0)
- moved R2 24.8 mm to (337.2, 43.7)
- moved SW_R1 24.8 mm to (339.0, 69.6)
- moved U1 24.8 mm to (351.7, 59.2)
- moved C2 24.8 mm to (356.5, 68.1)
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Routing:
- net ROW_3: track 0.00 -> 382.4 mm
- net ROW_5: track 0.00 -> 379.5 mm
- net ROW_7: track 0.00 -> 379.1 mm
- net ROW_1: track 0.00 -> 378.4 mm
- net ROW_2: track 0.00 -> 371.7 mm, vias 0 -> 18
- net ROW_6: track 0.00 -> 371.7 mm, vias 0 -> 16
- net ROW_4: track 0.00 -> 370.4 mm, vias 0 -> 16
- net ROW_9: track 88.0 -> 378.6 mm
- net ROW_8: track 84.6 -> 367.9 mm, vias 4 -> 16
